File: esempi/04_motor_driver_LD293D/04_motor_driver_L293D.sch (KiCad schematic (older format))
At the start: 27 parts, among them IC1 L293D, J1 Arduino_Nano_Header, P1 OUT12, P10 SER, P11 EXT_MOT, P2 ALIM_HALL, P4 OUT34, P5 HALL_01, P6 HOLE1, P7 HOLE2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

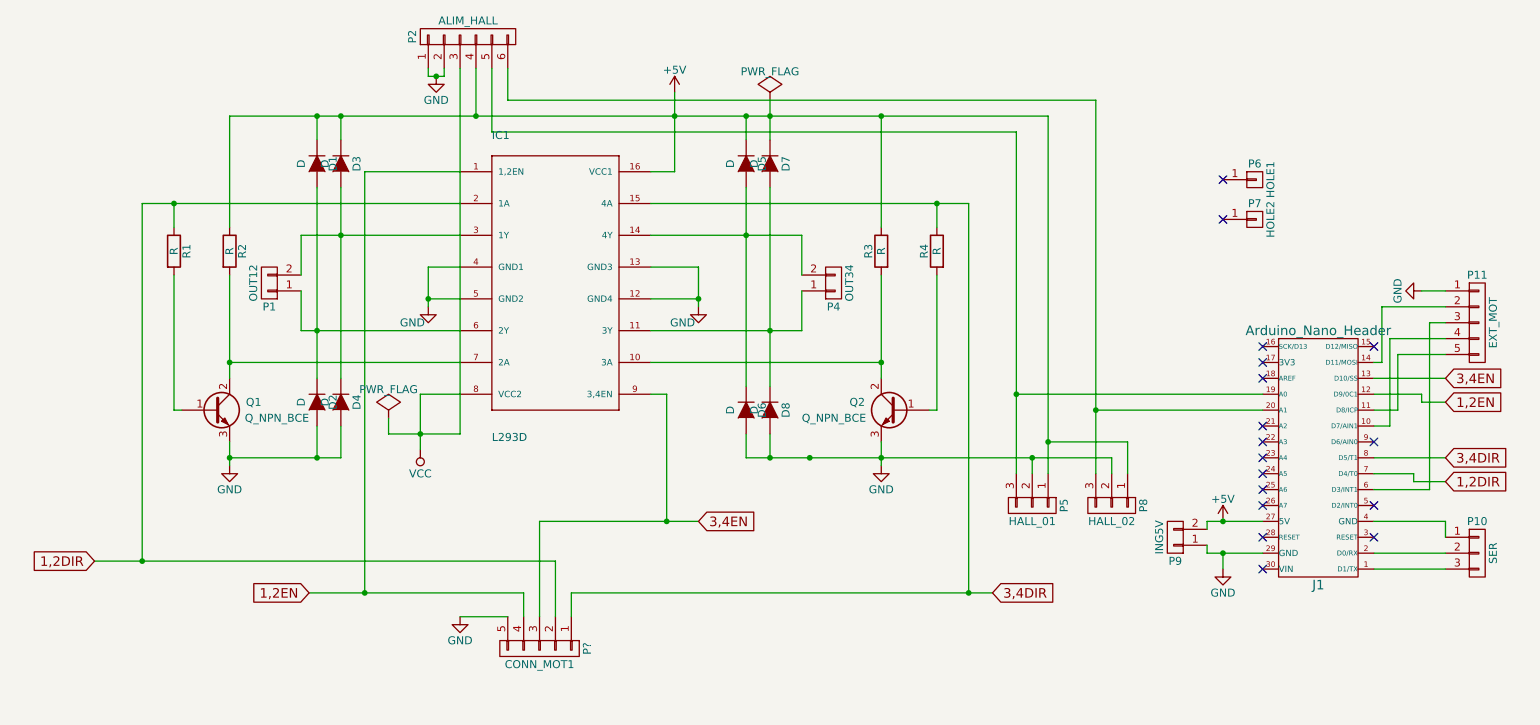
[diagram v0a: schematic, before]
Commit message: Creato portachiavi gadget raspibo logo
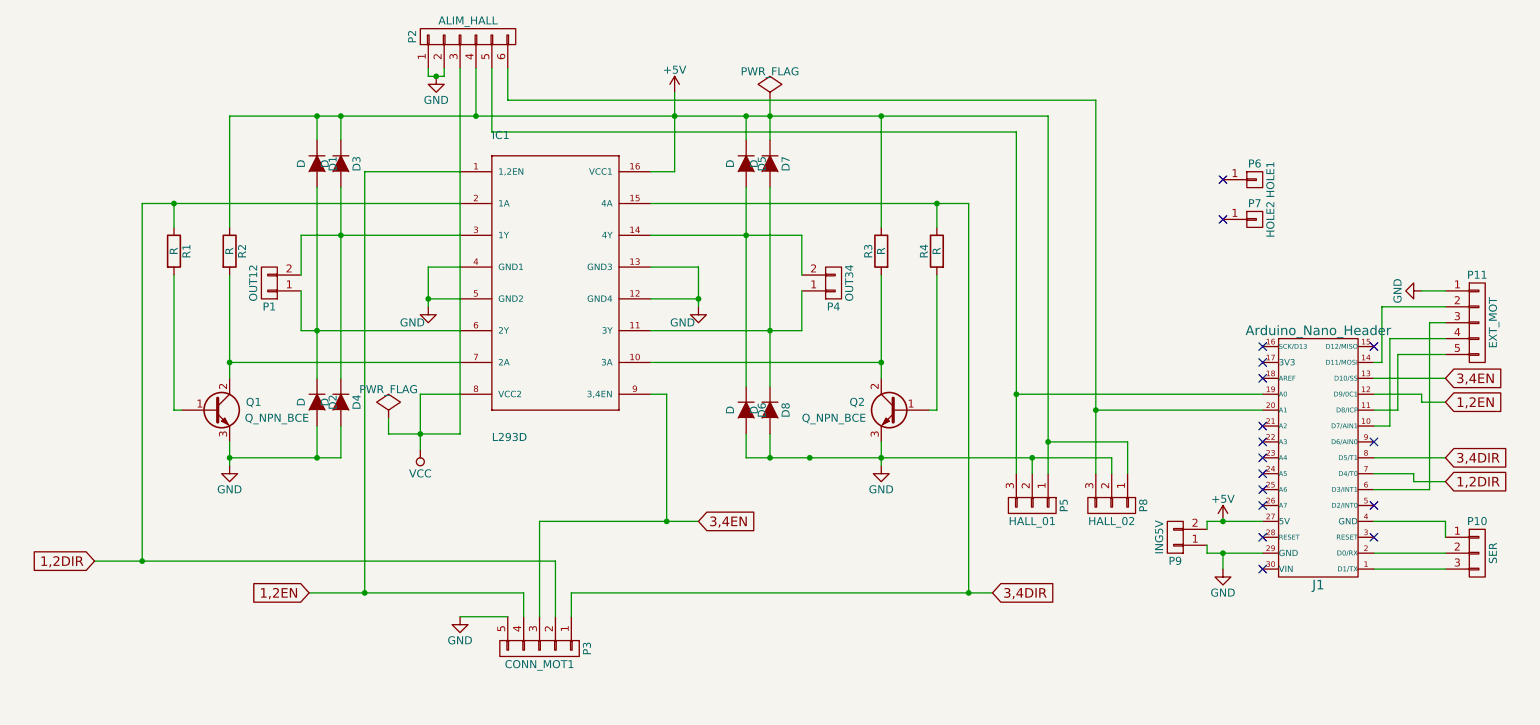
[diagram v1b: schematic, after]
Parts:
- P3: renamed from P?; footprint (none) -> w_pin_strip:pin_strip_5
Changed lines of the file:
@@
 $EndComp
 Wire Wire Line
-	3100 2750 3350 2750
-Wire Wire Line
-	3350 2750 4100 2750
-Wire Wire Line
-	3350 2450 3350 2750
-Wire Wire Line
-	3350 2750 3350 3650
+	3100 2750 4100 2750
+Wire Wire Line
+	3350 2450 3350 3650
 Wire Wire Line
 	3100 2750 3100 3000
 Wire Wire Line
-	5600 2950 5600 3150
-Wire Wire Line
-	5600 3150 5600 3200
+	5600 2950 5600 3200
 Wire Wire Line
 	5600 2950 5300 2950
@@
 	4100 2950 3900 2950
 Wire Wire Line
-	3900 2950 3900 3150
-Wire Wire Line
-	3900 3150 3900 3200
+	3900 2950 3900 3200
 Wire Wire Line
 	4100 3150 3900 3150
 Connection ~ 3900 3150
 Wire Wire Line
-	5450 1850 5450 2000
-Wire Wire Line
-	5450 2000 5450 2350
+	5450 1850 5450 2350
 Wire Wire Line
 	5450 2350 5300 2350
 Wire Wire Line
-	3850 3750 3850 4000
-Wire Wire Line
-	3850 4000 3850 4100
+	3850 3750 3850 4100
 Wire Wire Line
 	3850 3750 4100 3750
@@
 	2650 3550 4100 3550
 Wire Wire Line
-	2650 3000 2650 3550
-Wire Wire Line
-	2650 3550 2650 3650
+	2650 3000 2650 3650
 Connection ~ 2650 3550
 Wire Wire Line
@@
 Connection ~ 5450 2000
 Wire Wire Line
-	2100 2550 2300 2550
-Wire Wire Line
-	2300 2550 4100 2550
+	2100 2550 4100 2550
 Wire Wire Line
 	2300 2550 2300 2700
@@
 Connection ~ 2300 2550
 Wire Wire Line
-	5300 2750 5900 2750
-Wire Wire Line
-	5900 2750 6250 2750
-Wire Wire Line
-	6050 2450 6050 3350
-Wire Wire Line
-	6050 3350 6050 3700
-Wire Wire Line
-	5300 3350 6050 3350
-Wire Wire Line
-	6050 3350 6250 3350
+	5300 2750 6250 2750
+Wire Wire Line
+	6050 2450 6050 3700
+Wire Wire Line
+	5300 3350 6250 3350
 Wire Wire Line
 	6750 3550 5300 3550
 Wire Wire Line
-	6750 4050 6750 4150
-Wire Wire Line
-	6750 4150 6750 4200
-Wire Wire Line
-	6750 3000 6750 3550
-Wire Wire Line
-	6750 3550 6750 3650
+	6750 4050 6750 4200
+Wire Wire Line
+	6750 3000 6750 3650
 Connection ~ 6750 3550
 Wire Wire Line
 	6750 2000 6750 2700
 Wire Wire Line
-	5300 2550 7100 2550
-Wire Wire Line
-	7100 2550 7300 2550
+	5300 2550 7300 2550
 Wire Wire Line
 	7100 2550 7100 2700
@@
 Connection ~ 7100 2550
 Wire Wire Line
-	6050 1900 6050 2000
-Wire Wire Line
-	6050 2000 6050 2150
+	6050 1900 6050 2150
 Connection ~ 6050 2000
 Wire Wire Line
@@
 Connection ~ 3850 4000
 Wire Wire Line
-	2650 4050 2650 4150
-Wire Wire Line
-	2650 4150 2650 4200
-Wire Wire Line
-	5900 4150 6050 4150
-Wire Wire Line
-	6050 4150 6300 4150
-Wire Wire Line
-	6300 4150 6750 4150
-Wire Wire Line
-	6750 4150 7700 4150
-Wire Wire Line
-	7700 4150 8200 4150
+	2650 4050 2650 4200
+Wire Wire Line
+	5900 4150 8200 4150
 Connection ~ 6750 4150
 Connection ~ 6050 3350
@@
 	3200 3950 3200 4150
 Wire Wire Line
-	2650 4150 3200 4150
-Wire Wire Line
-	3200 4150 3350 4150
+	2650 4150 3350 4150
 Connection ~ 2650 4150
 Connection ~ 3200 3350
 Wire Wire Line
-	3100 3350 3200 3350
-Wire Wire Line
-	3200 3350 4100 3350
-Wire Wire Line
-	3200 2450 3200 3350
-Wire Wire Line
-	3200 3350 3200 3650
+	3100 3350 4100 3350
+Wire Wire Line
+	3200 2450 3200 3650
 Wire Wire Line
 	3100 3350 3100 3100
@@
 Connection ~ 5900 2000
 Wire Wire Line
-	5900 2450 5900 2750
-Wire Wire Line
-	5900 2750 5900 3700
+	5900 2450 5900 3700
 Wire Wire Line
 	5900 4000 5900 4150
@@
 	7300 2550 7300 5000
 Wire Wire Line
-	4800 5000 7300 5000
-Wire Wire Line
-	7300 5000 7450 5000
+	4800 5000 7450 5000
 Wire Wire Line
 	2100 2550 2100 4800
@@
 	5400 3750 5400 4550
 Wire Wire Line
-	4600 4550 5400 4550
-Wire Wire Line
-	5400 4550 5600 4550
+	4600 4550 5600 4550
 Wire Wire Line
 	4600 4550 4600 5150
 Wire Wire Line
-	1800 4800 2100 4800
-Wire Wire Line
-	2100 4800 4700 4800
+	1800 4800 4700 4800
 Wire Wire Line
 	4700 4800 4700 5150
@@
 	3500 2350 3500 5000
 Wire Wire Line
-	3150 5000 3500 5000
-Wire Wire Line
-	3500 5000 4500 5000
+	3150 5000 4500 5000
 Wire Wire Line
 	4200 2000 4200 1700
@@
 	4100 4000 4100 1700
 Wire Wire Line
-	3650 4000 3850 4000
-Wire Wire Line
-	3850 4000 4100 4000
+	3650 4000 4100 4000
 Wire Wire Line
 	4000 1750 4000 1700
 Wire Wire Line
-	3900 1750 3950 1750
-Wire Wire Line
-	3950 1750 4000 1750
+	3900 1750 4000 1750
 Wire Wire Line
 	3900 1700 3900 1750
 Connection ~ 3950 1750
 Wire Wire Line
-	7800 2000 7800 4050
-Wire Wire Line
-	7800 4050 7800 4250
+	7800 2000 7800 4250
 Connection ~ 6750 2000
 Wire Wire Line
-	7600 2100 7600 3750
-Wire Wire Line
-	7600 3750 7600 4250
+	7600 2100 7600 4250
 Wire Wire Line
 	4300 1700 4300 2100
@@
 Connection ~ 7800 4050
 Wire Wire Line
-	8100 1900 8100 3850
-Wire Wire Line
-	8100 3850 8100 4250
+	8100 1900 8100 4250
 Wire Wire Line
 	8100 1900 4400 1900
@@
 	4400 1900 4400 1700
 Wire Wire Line
-	8800 4550 8900 4550
-Wire Wire Line
-	8900 4550 9150 4550
+	8800 4550 9150 4550
 Wire Wire Line
 	9150 3750 7600 3750
@@
 Connection ~ 8100 3850
 Wire Wire Line
-	8800 4750 8900 4750
-Wire Wire Line
-	8900 4750 9150 4750
+	8800 4750 9150 4750
 Wire Wire Line
 	8900 4750 8900 4850
@@
 Connection ~ 7300 5000
 Wire Wire Line
-	2650 2000 3200 2000
-Wire Wire Line
-	3200 2000 3350 2000
-Wire Wire Line
-	3350 2000 4200 2000
-Wire Wire Line
-	4200 2000 5450 2000
-Wire Wire Line
-	5450 2000 5900 2000
-Wire Wire Line
-	5900 2000 6050 2000
-Wire Wire Line
-	6050 2000 6750 2000
-Wire Wire Line
-	6750 2000 7800 2000
+	2650 2000 7800 2000
 Text GLabel 10300 3800 2    60   Input ~ 0
 1,2EN
@@
 NoConn ~ 9850 4050
 $Comp
-L CONN_01X05 P?
+L CONN_01X05 P3
 U 1 1 558B3893
 P 4600 5350
-F 0 "P?" H 4600 5650 50  0000 C CNN
+F 0 "P3" H 4600 5650 50  0000 C CNN
 F 1 "CONN_MOT1" V 4700 5350 50  0000 C CNN
-F 2 "" H 4600 5350 60  0000 C CNN
+F 2 "w_pin_strip:pin_strip_5" H 4600 5350 60  0001 C CNN
 F 3 "" H 4600 5350 60  0000 C CNN
 	1    4600 5350
@@
 	4800 5000 4800 5150
 $Comp
-L GND #PWR?
+L GND #PWR013
 U 1 1 558B3B7C
 P 4100 5150
-F 0 "#PWR?" H 4100 4900 50  0001 C CNN
+F 0 "#PWR013" H 4100 4900 50  0001 C CNN
 F 1 "GND" H 4100 5000 50  0000 C CNN
 F 2 "" H 4100 5150 60  0000 C CNN

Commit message: Modifiche a Raspibo gadget e L293D
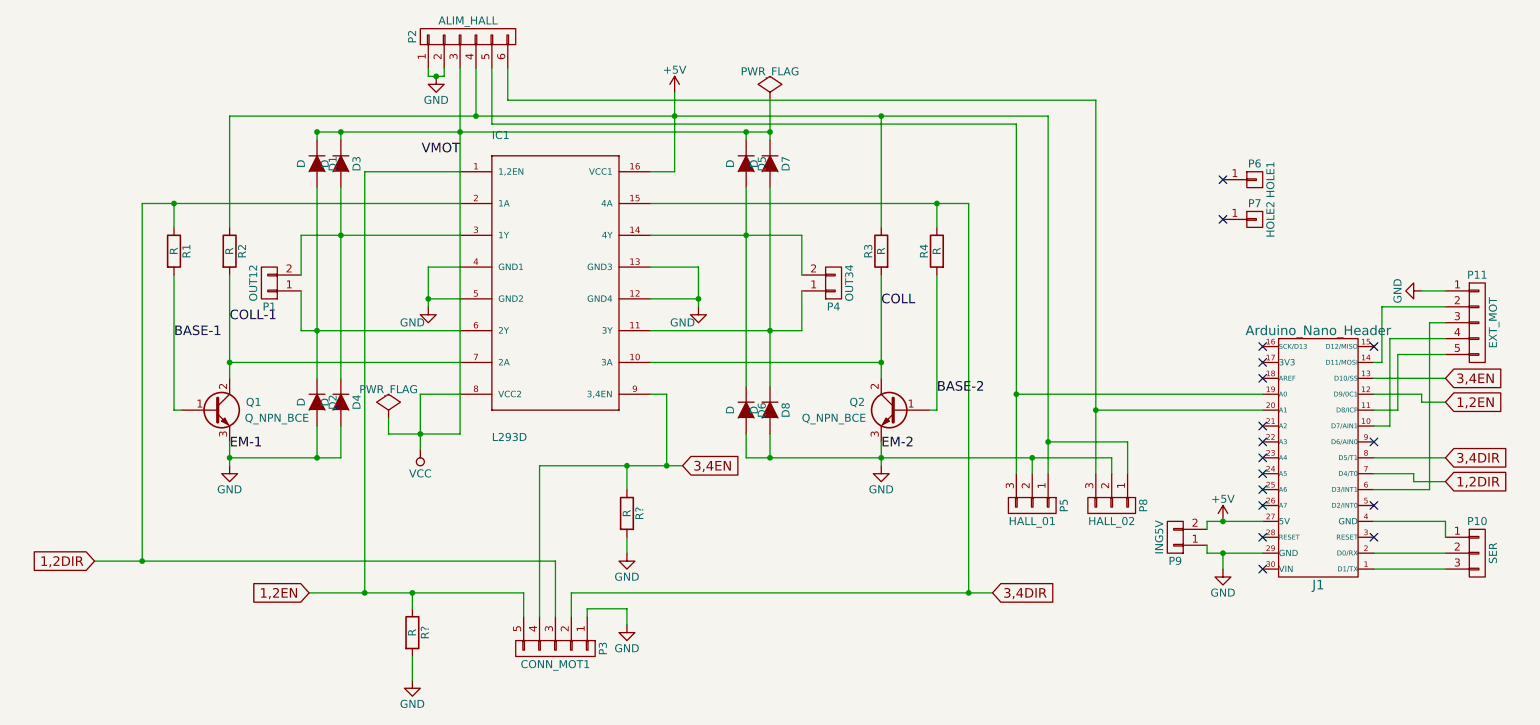
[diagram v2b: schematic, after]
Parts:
- added R? (x2): R, symbol R
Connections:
- net +5V: no longer D1.1 (K), D3.1 (K), D5.1 (K), D7.1 (K)
- net 1,2DIR: now also P3.3 (P3); no longer P3.2 (P2)
- net 1,2EN: now also P3.5 (P5), R?.1; no longer P3.4 (P4)
- net 3,4DIR: now also P3.2 (P2); no longer P3.1 (P1)
- net 3,4EN: now also P3.4 (P4), R?.1; no longer P3.3 (P3)
- net GND: now also P3.1 (P1), R?.2, R?.2; no longer P3.5 (P5)
- net VCC: now also D1.1 (K), D3.1 (K), D5.1 (K), D7.1 (K)
- net COLL: now reaches IC1.10 (3A), Q2.2 (C), R3.2
- net COLL-1: now reaches IC1.7 (2A), Q1.2 (C), R2.2
- net BASE-1: now reaches Q1.1 (B), R1.2
- net BASE-2: now reaches Q2.1 (B), R4.2
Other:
- moved on the sheet: P3

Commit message: Allineamento files per pubblicazione su wiki
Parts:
- R5, R6: renamed from R?; footprint (none) -> w_smd_resistors:r_0805
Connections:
- net GND: now also J1.4 (GND), P10.1 (P1)
- net TX: now reaches J1.1 (D1/TX), P10.3 (P3)
- net RX: now reaches J1.2 (D0/RX), P10.2 (P2)
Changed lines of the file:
@@
 	5150 5100 5150 5200
 $Comp
-L R R?
+L R R5
 U 1 1 55C8D122
 P 3800 5250
-F 0 "R?" V 3880 5250 50  0000 C CNN
+F 0 "R5" V 3880 5250 50  0000 C CNN
 F 1 "R" V 3800 5250 50  0000 C CNN
-F 2 "" V 3730 5250 30  0000 C CNN
+F 2 "w_smd_resistors:r_0805" V 3730 5250 30  0001 C CNN
 F 3 "" H 3800 5250 30  0000 C CNN
 	1    3800 5250
@@
 $EndComp
 $Comp
-L R R?
+L R R6
 U 1 1 55C8D23B
 P 5150 4500
-F 0 "R?" V 5230 4500 50  0000 C CNN
+F 0 "R6" V 5230 4500 50  0000 C CNN
 F 1 "R" V 5150 4500 50  0000 C CNN
-F 2 "" V 5080 4500 30  0000 C CNN
+F 2 "w_smd_resistors:r_0805" V 5080 4500 30  0001 C CNN
 F 3 "" H 5150 4500 30  0000 C CNN
 	1    5150 4500
@@
 Connection ~ 3800 5000
 $Comp
-L GND #PWR?
+L GND #PWR014
 U 1 1 55C8D5B3
 P 3800 5550
-F 0 "#PWR?" H 3800 5300 50  0001 C CNN
+F 0 "#PWR014" H 3800 5300 50  0001 C CNN
 F 1 "GND" H 3800 5400 50  0000 C CNN
 F 2 "" H 3800 5550 60  0000 C CNN
@@
 	3800 5550 3800 5400
 $Comp
-L GND #PWR?
+L GND #PWR015
 U 1 1 55C8D6BB
 P 5150 4750
-F 0 "#PWR?" H 5150 4500 50  0001 C CNN
+F 0 "#PWR015" H 5150 4500 50  0001 C CNN
 F 1 "GND" H 5150 4600 50  0000 C CNN
 F 2 "" H 5150 4750 60  0000 C CNN
@@
 Wire Wire Line
 	5150 4750 5150 4650
+Text Label 10000 4750 0    60   ~ 0
+RX
+Text Label 10000 4850 0    60   ~ 0
+TX
+Text Label 10000 4550 0    60   ~ 0
+GND
 $EndSCHEMATC
